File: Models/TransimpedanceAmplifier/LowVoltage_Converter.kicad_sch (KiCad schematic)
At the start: 3 parts, among them U10 LM7805, 5V, 5%, U8 TLV76133, 3.3V, 1%

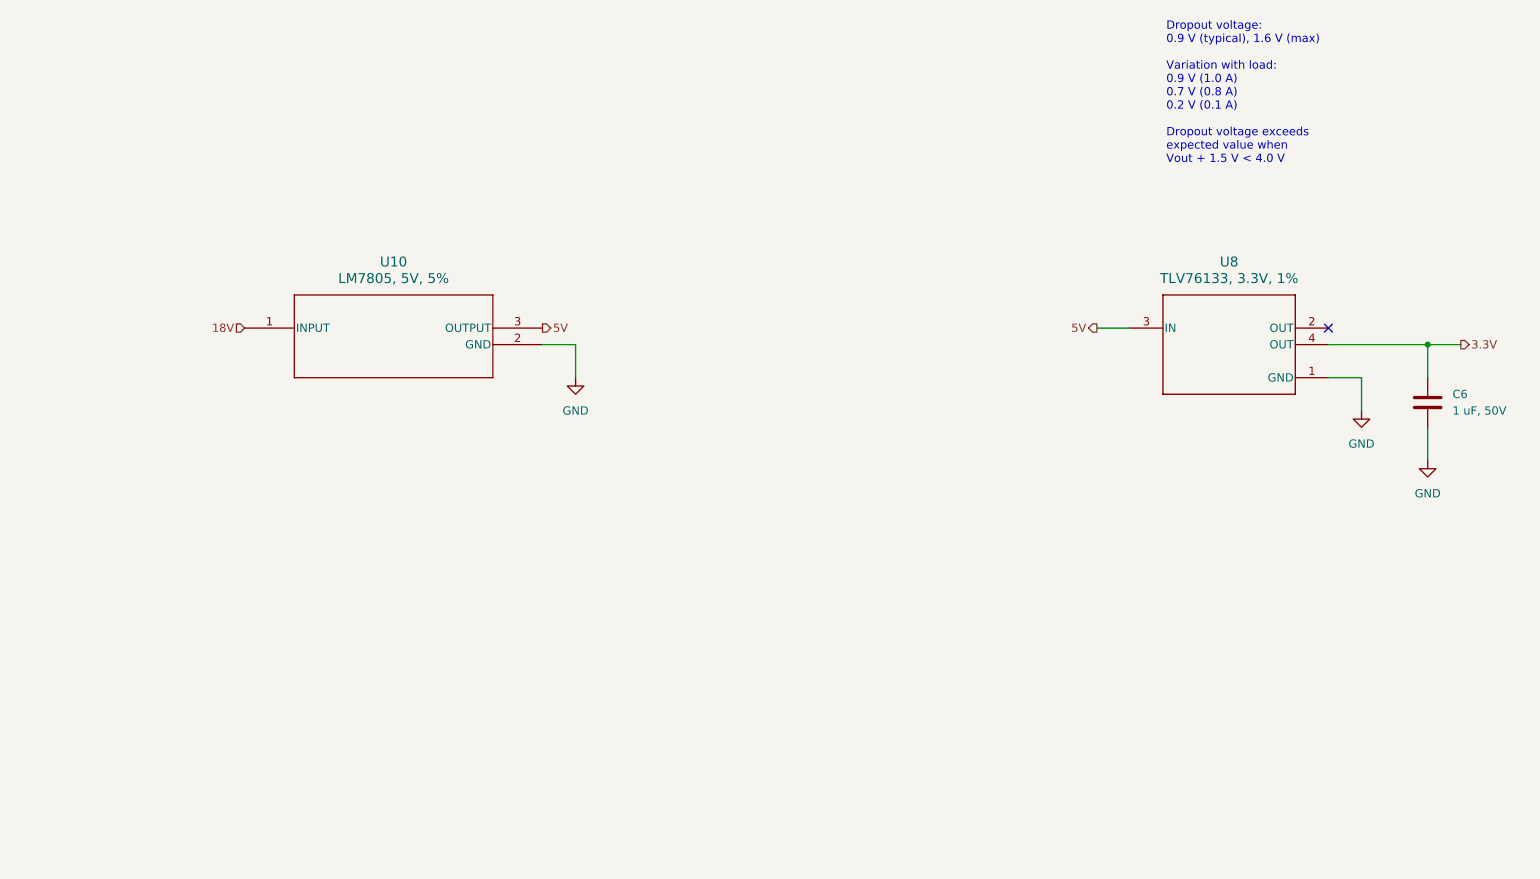
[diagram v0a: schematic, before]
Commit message: Finished the decoupling networks for the power subsystem
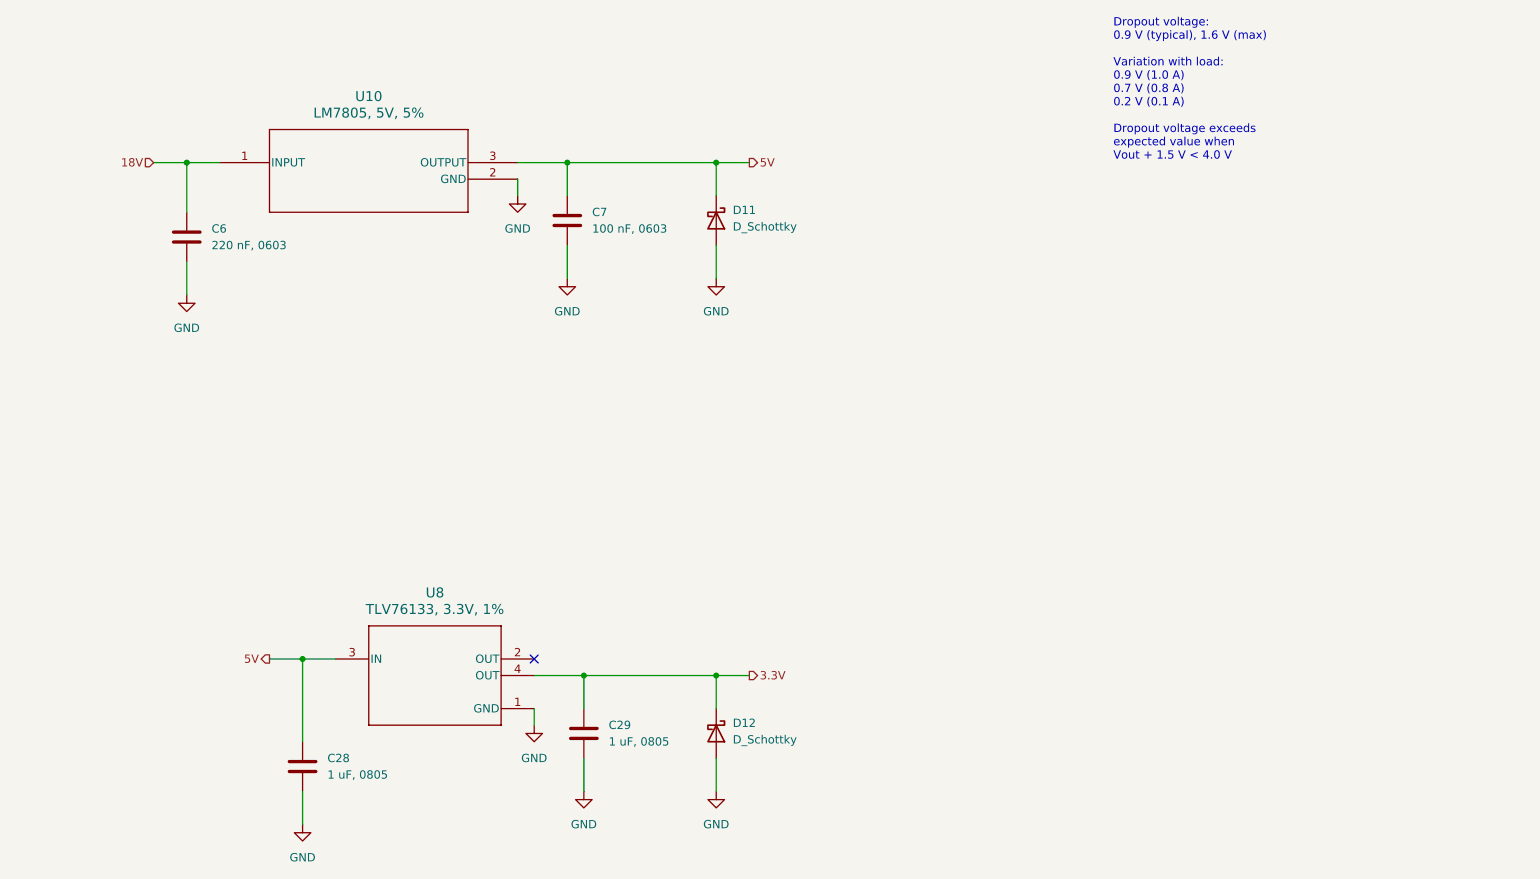
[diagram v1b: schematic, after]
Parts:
- added C28, C29: 1 uF, 0805, symbol Device:C
- added C7: 100 nF, 0603, symbol Device:C
- added D11, D12: D_Schottky, symbol Device:D_Schottky
- C6: value 1 uF, 50V -> 220 nF, 0603; Purchase Link https://www.digikey.com/en/products/detail/murata-electroni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 -> (none)
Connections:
- net 18V: now also C6.1
- net 3.3V: now also C29.1, D12.1 (K); no longer C6.1
- net 5V: now also C28.1, C7.1, D11.1 (K)
- net GND: now also C28.2, C29.2, C7.2, D11.2 (A), D12.2 (A)
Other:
- moved on the sheet: U8

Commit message: Finished for today
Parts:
- C28, C29, C6, C7: Purchase Link (none) -> https://www.digikey.com/en/products/detail/murata-electroni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
- D11, D12: Purchase Link (none) -> https://www.digikey.com/en/products/detail/diodes-incorpora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
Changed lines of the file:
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@@
 	(text "Dropout voltage:\n0.9 V (typical), 1.6 V (max)\n\nVariation with load:\n0.9 V (1.0 A)\n0.7 V (0.8 A)\n0.2 V (0.1 A)\n\nDropout voltage exceeds\nexpected value when\nVout + 1.5 V < 4.0 V"
 		(exclude_from_sim no)
-		(at 195.58 44.704 0)
+		(at 26.67 147.066 0)
 		(effects
 			(font
@@
 			)
 		)
+		(property "Purchase Link" "https://www.digikey.com/en/products/detail/murata-electronics/GRT21BR71H105KE01L/10702345"
+			(at 114.3 143.51 0)
+			(effects
+				(font
+					(size 1.27 1.27)
+				)
+				(hide yes)
+			)
+		)
 		(pin "1"
 		)
@@
 			)
 		)
+		(property "Purchase Link" "https://www.digikey.com/en/products/detail/diodes-incorporated/1N5819HW-7-F/814970"
+			(at 134.62 64.77 90)
+			(effects
+				(font
+					(size 1.27 1.27)
+				)
+				(hide yes)
+			)
+		)
 		(pin "1"
 		)
@@
 			)
 		)
+		(property "Purchase Link" "https://www.digikey.com/en/products/detail/murata-electronics/GRT21BR71H105KE01L/10702345"
+			(at 71.12 148.59 0)
+			(effects
+				(font
+					(size 1.27 1.27)
+				)
+				(hide yes)
+			)
+		)
 		(pin "1"
 		)
@@
 			)
 		)
+		(property "Purchase Link" "https://www.digikey.com/en/products/detail/murata-electronics/GRM188R71H224KAC4D/5797498"
+			(at 53.34 67.31 0)
+			(effects
+				(font
+					(size 1.27 1.27)
+				)
+				(hide yes)
+			)
+		)
 		(pin "2"
 		)
@@
 			)
 		)
+		(property "Purchase Link" "https://www.digikey.com/en/products/detail/diodes-incorporated/1N5819HW-7-F/814970"
+			(at 134.62 143.51 90)
+			(effects
+				(font
+					(size 1.27 1.27)
+				)
+				(hide yes)
+			)
+		)
 		(pin "1"
 		)
@@
 			(at 111.76 64.77 0)
 			(effects
+				(font
+					(size 1.27 1.27)
+				)
+				(hide yes)
+			)
+		)
+		(property "Purchase Link" "https://www.digikey.com/en/products/detail/murata-electronics/GRM188R72A104KA35D/702549"
+			(at 111.76 64.77 0)
+			(effects

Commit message: Save progress
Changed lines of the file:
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@@
 	)
 	(symbol
+		(lib_name "D_Schottky_1")
 		(lib_id "Device:D_Schottky")
 		(at 134.62 64.77 270)

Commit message: Save progress
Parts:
- U10: footprint NDE3_TEX -> (none)
- U8: footprint DCY0004A-IPC_A -> (none)
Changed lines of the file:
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@@
 			)
 		)
-		(property "Footprint" "NDE3_TEX"
+		(property "Footprint" ""
 			(at 58.42 55.88 0)
 			(effects
@@
 			)
 		)
-		(property "Footprint" "DCY0004A-IPC_A"
+		(property "Footprint" ""
 			(at 77.47 130.81 0)
 			(effects

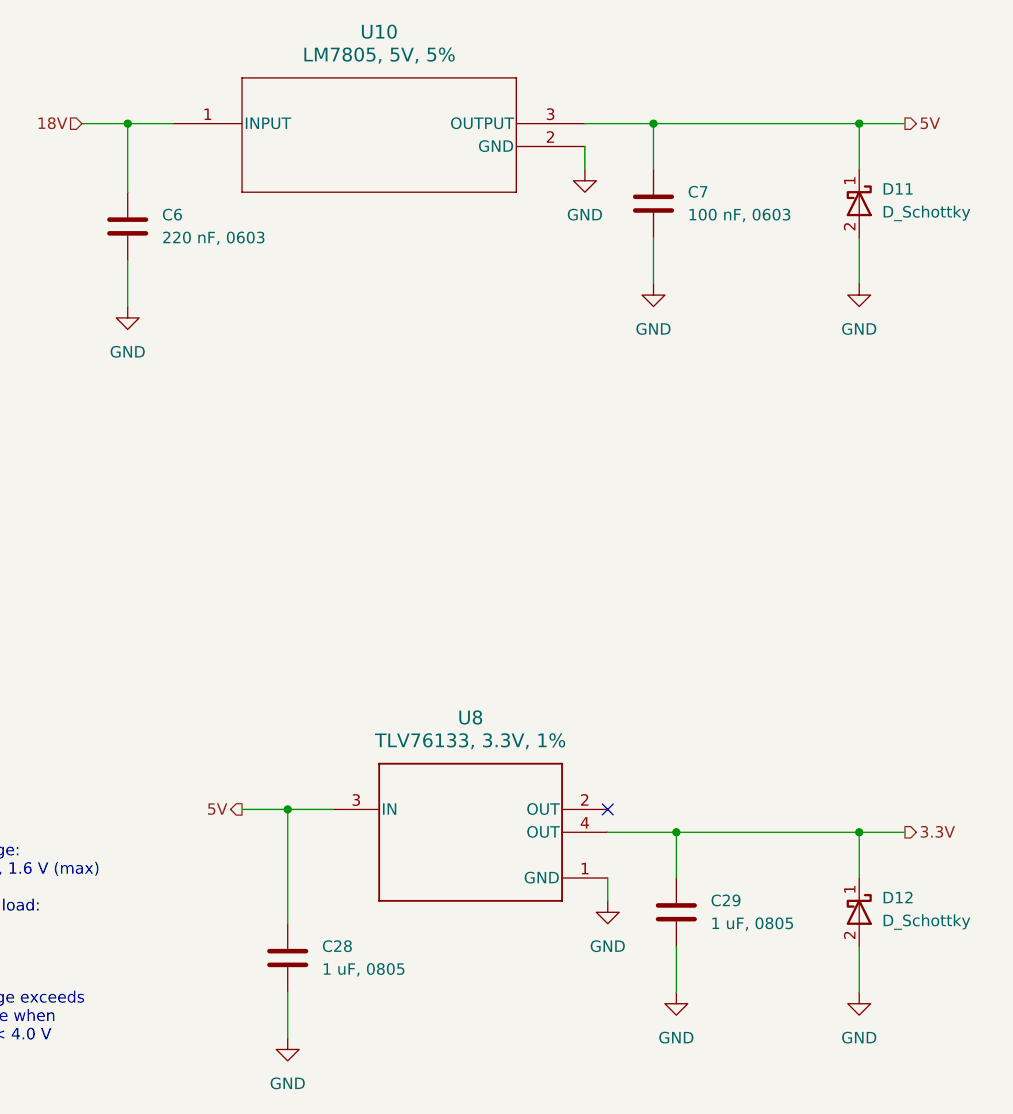
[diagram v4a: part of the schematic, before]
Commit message: Overhauled all of the annotations
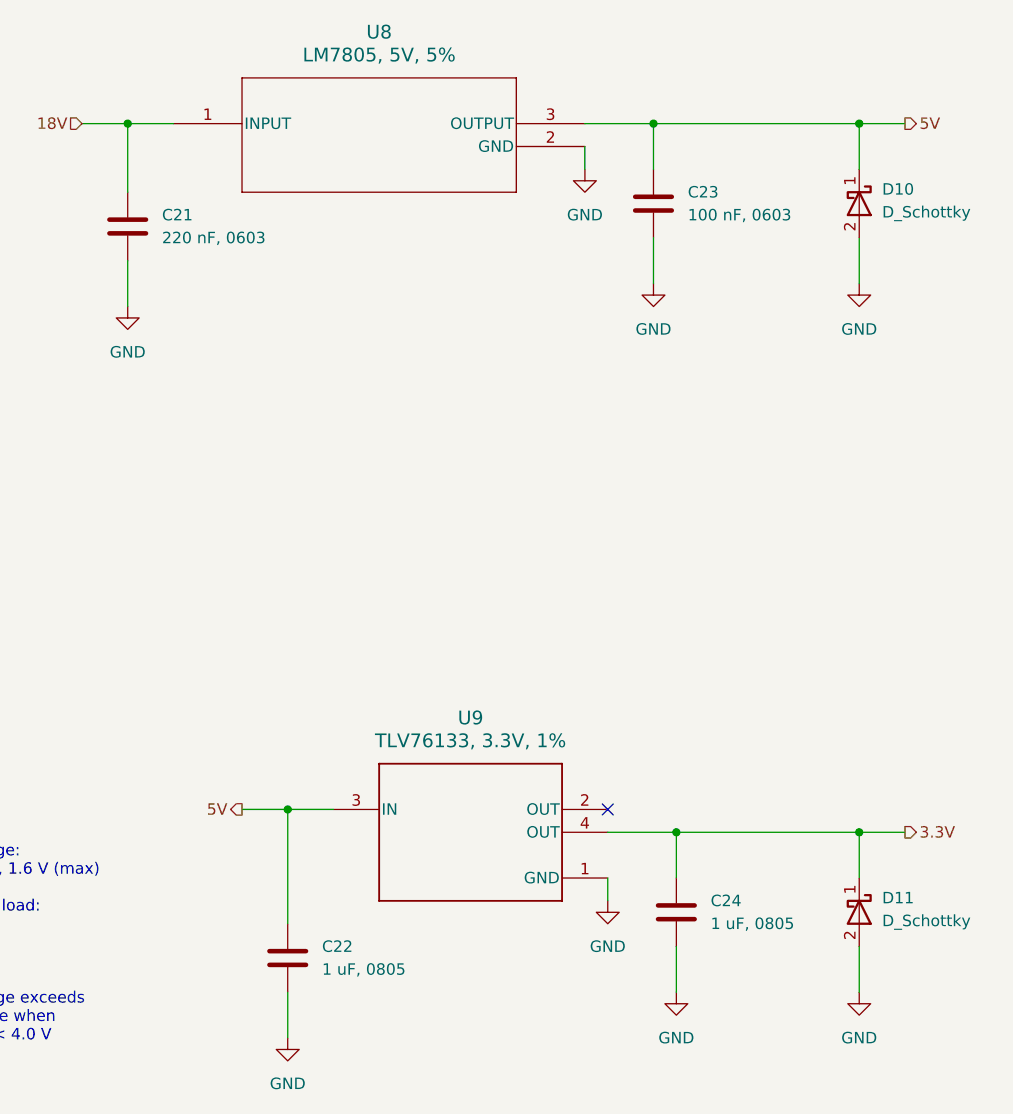
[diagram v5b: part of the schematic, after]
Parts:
- renumbered C6 to C21, C28 to C22, C7 to C23, C29 to C24, D11 to D10, D12 to D11, U10 to U8, U8 to U9
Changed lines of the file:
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@@
 		(dnp no)
 		(fields_autoplaced yes)
-		(property "Reference" "C29"
+		(property "Reference" "C24"
 			(at 118.11 142.2399 0)
 			(effects
@@
 			(project ""
 				(path "/ec9f2ae3-e40d-40eb-9760-2b611ee8efd1/d0ece2d4-5b22-4822-ad0c-e2361683ec3d/8db21157-4c7b-40b0-8814-5c9be8b7a36f"
-					(reference "C29")
+					(reference "C24")
 					(unit 1)
 				)
@@
 		(dnp no)
 		(fields_autoplaced yes)
-		(property "Reference" "U10"
+		(property "Reference" "U8"
 			(at 81.28 45.72 0)
 			(effects
@@
 			(project "TransimpedanceAmplifier"
 				(path "/ec9f2ae3-e40d-40eb-9760-2b611ee8efd1/d0ece2d4-5b22-4822-ad0c-e2361683ec3d/8db21157-4c7b-40b0-8814-5c9be8b7a36f"
-					(reference "U10")
+					(reference "U8")
 					(unit 1)
 				)
@@
 		(dnp no)
 		(fields_autoplaced yes)
-		(property "Reference" "#PWR012"
+		(property "Reference" "#PWR033"
 			(at 106.68 148.59 0)
 			(effects
@@
 			(project ""
 				(path "/ec9f2ae3-e40d-40eb-9760-2b611ee8efd1/d0ece2d4-5b22-4822-ad0c-e2361683ec3d/8db21157-4c7b-40b0-8814-5c9be8b7a36f"
-					(reference "#PWR012")
+					(reference "#PWR033")
 					(unit 1)
 				)
@@
 		(dnp no)
 		(fields_autoplaced yes)
-		(property "Reference" "D11"
+		(property "Reference" "D10"
 			(at 137.16 63.1824 90)
 			(effects
@@
 			(project "TransimpedanceAmplifier"
 				(path "/ec9f2ae3-e40d-40eb-9760-2b611ee8efd1/d0ece2d4-5b22-4822-ad0c-e2361683ec3d/8db21157-4c7b-40b0-8814-5c9be8b7a36f"
-					(reference "D11")
+					(reference "D10")
 					(unit 1)
 				)
@@
 		(dnp no)
 		(fields_autoplaced yes)
-		(property "Reference" "#PWR021"
+		(property "Reference" "#PWR036"
 			(at 134.62 80.01 0)
 			(effects
@@
 			(project "TransimpedanceAmplifier"
 				(path "/ec9f2ae3-e40d-40eb-9760-2b611ee8efd1/d0ece2d4-5b22-4822-ad0c-e2361683ec3d/8db21157-4c7b-40b0-8814-5c9be8b7a36f"
-					(reference "#PWR021")
+					(reference "#PWR036")
 					(unit 1)
 				)
@@
 		(dnp no)
 		(fields_autoplaced yes)
-		(property "Reference" "#PWR014"
+		(property "Reference" "#PWR030"
 			(at 53.34 82.55 0)
 			(effects
@@
 			(project "TransimpedanceAmplifier"
 				(path "/ec9f2ae3-e40d-40eb-9760-2b611ee8efd1/d0ece2d4-5b22-4822-ad0c-e2361683ec3d/8db21157-4c7b-40b0-8814-5c9be8b7a36f"
-					(reference "#PWR014")
+					(reference "#PWR030")
 					(unit 1)
 				)
@@
 		(dnp no)
 		(fields_autoplaced yes)
-		(property "Reference" "#PWR034"
+		(property "Reference" "#PWR031"
 			(at 71.12 163.83 0)
 			(effects
@@
 			(project ""
 				(path "/ec9f2ae3-e40d-40eb-9760-2b611ee8efd1/d0ece2d4-5b22-4822-ad0c-e2361683ec3d/8db21157-4c7b-40b0-8814-5c9be8b7a36f"
-					(reference "#PWR034")
+					(reference "#PWR031")
 					(unit 1)
 				)
@@
 		(dnp no)
 		(fields_autoplaced yes)
-		(property "Reference" "C28"
+		(property "Reference" "C22"
 			(at 74.93 147.3199 0)
 			(effects
@@
 			(project ""
 				(path "/ec9f2ae3-e40d-40eb-9760-2b611ee8efd1/d0ece2d4-5b22-4822-ad0c-e2361683ec3d/8db21157-4c7b-40b0-8814-5c9be8b7a36f"
-					(reference "C28")
+					(reference "C22")
 					(unit 1)
 				)
@@
 		(dnp no)
 		(fields_autoplaced yes)
-		(property "Reference" "#PWR020"
+		(property "Reference" "#PWR034"
 			(at 111.76 80.01 0)
 			(effects
@@
 			(project "TransimpedanceAmplifier"
 				(path "/ec9f2ae3-e40d-40eb-9760-2b611ee8efd1/d0ece2d4-5b22-4822-ad0c-e2361683ec3d/8db21157-4c7b-40b0-8814-5c9be8b7a36f"
-					(reference "#PWR020")
+					(reference "#PWR034")
 					(unit 1)
 				)
@@
 		(dnp no)
 		(fields_autoplaced yes)
-		(property "Reference" "#PWR030"
+		(property "Reference" "#PWR037"
 			(at 134.62 158.75 0)
 			(effects
@@
 			(project ""
 				(path "/ec9f2ae3-e40d-40eb-9760-2b611ee8efd1/d0ece2d4-5b22-4822-ad0c-e2361683ec3d/8db21157-4c7b-40b0-8814-5c9be8b7a36f"
-					(reference "#PWR030")
+					(reference "#PWR037")
 					(unit 1)
 				)
@@
 		(dnp no)
 		(fields_autoplaced yes)
-		(property "Reference" "C6"
+		(property "Reference" "C21"
 			(at 57.15 66.0399 0)
 			(effects
@@
 			(project "TransimpedanceAmplifier"
 				(path "/ec9f2ae3-e40d-40eb-9760-2b611ee8efd1/d0ece2d4-5b22-4822-ad0c-e2361683ec3d/8db21157-4c7b-40b0-8814-5c9be8b7a36f"
-					(reference "C6")
+					(reference "C21")
 					(unit 1)
 				)
@@
 		(dnp no)
 		(fields_autoplaced yes)
-		(property "Reference" "D12"
+		(property "Reference" "D11"
 			(at 137.16 141.9224 90)
 			(effects
@@
 			(project ""
 				(path "/ec9f2ae3-e40d-40eb-9760-2b611ee8efd1/d0ece2d4-5b22-4822-ad0c-e2361683ec3d/8db21157-4c7b-40b0-8814-5c9be8b7a36f"
-					(reference "D12")
+					(reference "D11")
 					(unit 1)
 				)
@@
 		(dnp no)
 		(fields_autoplaced yes)
-		(property "Reference" "#PWR022"
+		(property "Reference" "#PWR035"
 			(at 114.3 158.75 0)
 			(effects
@@
 			(project ""
 				(path "/ec9f2ae3-e40d-40eb-9760-2b611ee8efd1/d0ece2d4-5b22-4822-ad0c-e2361683ec3d/8db21157-4c7b-40b0-8814-5c9be8b7a36f"
-					(reference "#PWR022")
+					(reference "#PWR035")
 					(unit 1)
 				)
@@
 		(dnp no)
 		(fields_autoplaced yes)
-		(property "Reference" "#PWR015"
+		(property "Reference" "#PWR032"
 			(at 104.14 67.31 0)
 			(effects
@@
 			(project "TransimpedanceAmplifier"
 				(path "/ec9f2ae3-e40d-40eb-9760-2b611ee8efd1/d0ece2d4-5b22-4822-ad0c-e2361683ec3d/8db21157-4c7b-40b0-8814-5c9be8b7a36f"
-					(reference "#PWR015")
+					(reference "#PWR032")
 					(unit 1)
 				)
@@
 		(dnp no)
 		(fields_autoplaced yes)
-		(property "Reference" "C7"
+		(property "Reference" "C23"
 			(at 115.57 63.4999 0)
 			(effects
@@
 			(project "TransimpedanceAmplifier"
 				(path "/ec9f2ae3-e40d-40eb-9760-2b611ee8efd1/d0ece2d4-5b22-4822-ad0c-e2361683ec3d/8db21157-4c7b-40b0-8814-5c9be8b7a36f"
-					(reference "C7")
+					(reference "C23")
 					(unit 1)
 				)
@@
 		(dnp no)
 		(fields_autoplaced yes)
-		(property "Reference" "U8"
+		(property "Reference" "U9"
 			(at 91.44 121.92 0)
 			(effects
@@
 			(project ""
 				(path "/ec9f2ae3-e40d-40eb-9760-2b611ee8efd1/d0ece2d4-5b22-4822-ad0c-e2361683ec3d/8db21157-4c7b-40b0-8814-5c9be8b7a36f"
-					(reference "U8")
-					(unit 1)
-				)
+					(reference "U9")
+					(unit 1)
+				)
